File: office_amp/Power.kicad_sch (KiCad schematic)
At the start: 27 parts, among them J1 Jack-DC, Q1 DMT6012LSS, U1 LM74700, U2 TBA_2-2421, U4 TBA_2-2421

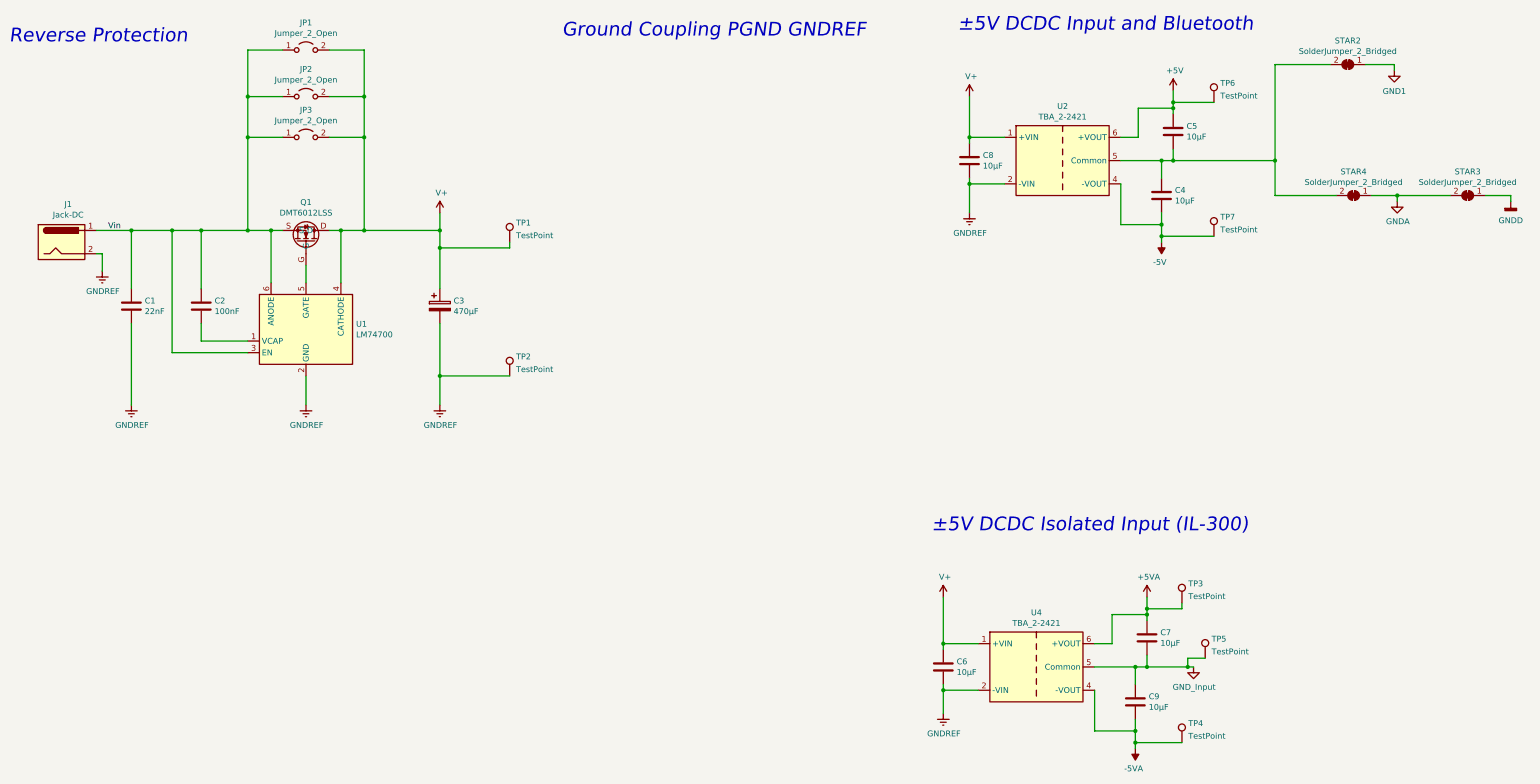
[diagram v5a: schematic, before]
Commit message: Added CHanges from Testing, first layout V1.5
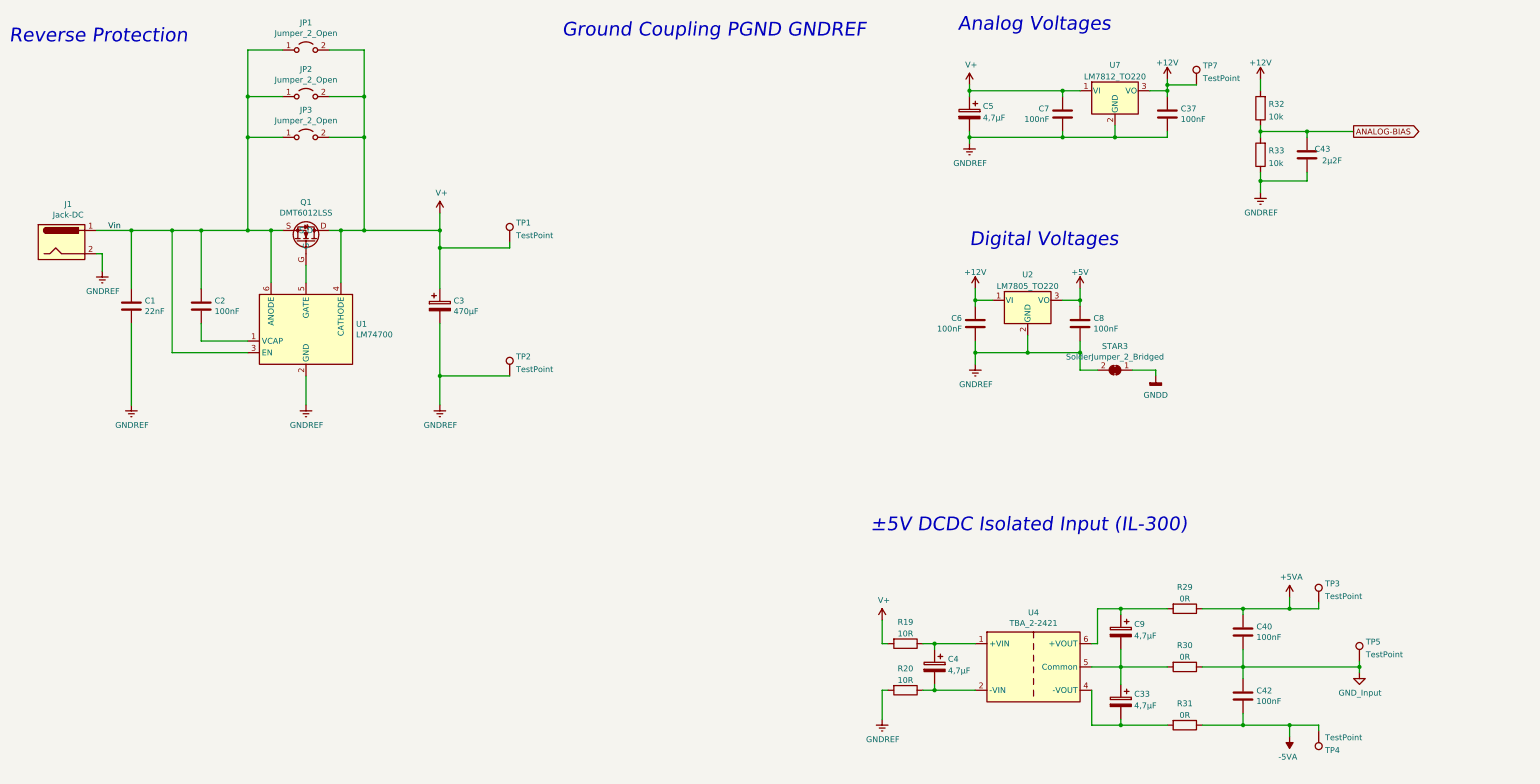
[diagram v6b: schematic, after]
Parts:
- removed C4, C5, C9: 10µF, Capacitor_SMD:C_0805_2012Metric_Pad1.18x1.45mm_HandSolder, symbol Device:C
- removed STAR2, STAR4: SolderJumper_2_Bridged, Jumper:SolderJumper-2_P1.3mm_Bridged_RoundedPad1.0x1.5mm, symbol Jumper:SolderJumper_2_Bridged
- removed TP6: TestPoint, TestPoint:TestPoint_Pad_D1.0mm, symbol Connector:TestPoint
- removed U2: TBA_2-2421, office_amp:SIP-7, symbol MyLib:TBA_2-XXXX
- added C33, C4, C5, C9: 4,7µF, Capacitor_THT:CP_Radial_D5.0mm_P2.00mm, symbol Device:C_Polarized
- added C37, C40, C42: 100nF, Capacitor_SMD:C_0805_2012Metric_Pad1.18x1.45mm_HandSolder, symbol Device:C
- added C43: 2µ2F, Capacitor_SMD:C_0805_2012Metric_Pad1.18x1.45mm_HandSolder, symbol Device:C
- added R19, R20: 10R, Resistor_SMD:R_0805_2012Metric_Pad1.20x1.40mm_HandSolder, symbol Device:R
- added R29, R30, R31: 0R, Resistor_SMD:R_0805_2012Metric_Pad1.20x1.40mm_HandSolder, symbol Device:R
- added R32, R33: 10k, Resistor_SMD:R_0805_2012Metric_Pad1.20x1.40mm_HandSolder, symbol Device:R
- added U2: LM7805_TO220, Package_TO_SOT_THT:TO-220-3_Vertical, symbol Regulator_Linear:LM7805_TO220
- added U7: LM7812_TO220, Package_TO_SOT_THT:TO-220-3_Vertical, symbol Regulator_Linear:LM7812_TO220
- C6, C7, C8: value 10µF -> 100nF
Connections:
- net GNDA is gone; now on net GNDREF: STAR3.2 (B)
- net +5V: now also C8.1, U2.3 (VO)
- net +5VA: now also C40.1, R29.1; no longer C7.1, U4.6 (+VOUT)
- net -5VA: now also C42.2, R31.1; no longer U4.4 (-VOUT)
- net GNDREF: now also C7.2, C37.2, C43.1, C5.2, R20.2, R33.1, U2.2 (GND), U7.2 (GND); no longer U4.2 (-VIN)
- net GND_Input: now also C40.2, C42.1, R30.1; no longer C7.2, U4.5 (Common)
- net V+: now also C7.1, C5.1, R19.2, U7.1 (VI); no longer C6.1, C8.1, U4.1 (+VIN)
- net -5V renamed +12V
- net +12V: now also C6.1, C37.1, R32.2, U2.1 (VI), U7.3 (VO)
- new net: C4.1, R19.1, U4.1 (+VIN)
- new net: C4.2, R20.1, U4.2 (-VIN)
- new net: C33.2, R31.2, U4.4 (-VOUT)
- new net: C33.1, C9.2, R30.2, U4.5 (Common)
- new net: C9.1, R29.2, U4.6 (+VOUT)
- new net ANALOG-BIAS: C43.2, R32.1, R33.2
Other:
- note added: "Analog Voltages"
- note added: "Digital Voltages"
- note removed: "±5V DCDC Input and Bluetooth"
- moved on the sheet: STAR3, TP3, TP4, TP5, TP7, U4

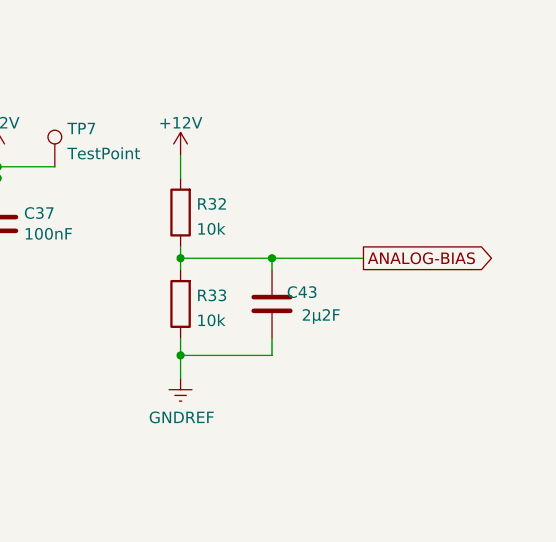
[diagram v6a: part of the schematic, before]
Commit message: Organized Schematic
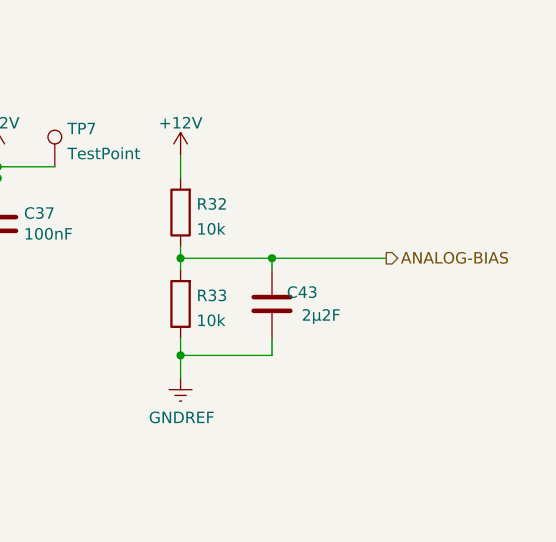
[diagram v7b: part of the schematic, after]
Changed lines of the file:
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@@
   (junction (at 113.03 69.85) (diameter 0) (color 0 0 0 0)
   )
+  (junction (at 302.26 48.26) (diameter 0) (color 0 0 0 0)
+  )
   (junction (at 298.45 177.8) (diameter 0) (color 0 0 0 0)
   )
@@
   (junction (at 260.35 49.53) (diameter 0) (color 0 0 0 0)
   )
-  (junction (at 302.26 48.26) (diameter 0) (color 0 0 0 0)
-  )
   (junction (at 71.12 49.53) (diameter 0) (color 0 0 0 0)
   )
@@
     (stroke (width 0) (type default) (color 0 0 0 0))
   )
-  (wire (pts (xy 302.26 48.26) (xy 312.42 48.26))
-    (stroke (width 0) (type default) (color 0 0 0 0))
-  )
   (wire (pts (xy 292.1 59.055) (xy 292.1 61.595))
     (stroke (width 0) (type default) (color 0 0 0 0))
@@
   )
   (wire (pts (xy 304.8 152.4) (xy 304.8 151.13))
+    (stroke (width 0) (type default) (color 0 0 0 0))
+  )
+  (wire (pts (xy 302.26 48.26) (xy 314.96 48.26))
     (stroke (width 0) (type default) (color 0 0 0 0))
   )
@@
     (effects (font (size 1.27 1.27)) (justify left bottom))
   )
-  (global_label "ANALOG-BIAS" (shape output) (at 312.42 48.26 0) (fields_autoplaced)
+  (hierarchical_label "ANALOG-BIAS" (shape output) (at 314.96 48.26 0)
     (effects (font (size 1.27 1.27)) (justify left))
-    (property "Intersheet References" "${INTERSHEET_REFS}" (id 0) (at 327.6256 48.1806 0)
-      (effects (font (size 1.27 1.27)) (justify left) hide)
-    )
   )
   (symbol (lib_id "Power_Management:LM74700") (at 83.82 91.44 0) (unit 1)

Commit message: new test software
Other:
- moved on the sheet: C43, R32, R33
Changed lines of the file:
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@@
   (junction (at 288.29 152.4) (diameter 0) (color 0 0 0 0)
   )
-  (junction (at 292.1 59.055) (diameter 0) (color 0 0 0 0)
+  (junction (at 299.72 59.055) (diameter 0) (color 0 0 0 0)
   )
   (junction (at 113.03 73.66) (diameter 0) (color 0 0 0 0)
@@
   (junction (at 113.03 69.85) (diameter 0) (color 0 0 0 0)
   )
-  (junction (at 302.26 48.26) (diameter 0) (color 0 0 0 0)
+  (junction (at 309.88 48.26) (diameter 0) (color 0 0 0 0)
   )
   (junction (at 298.45 177.8) (diameter 0) (color 0 0 0 0)
@@
   (junction (at 76.2 69.85) (diameter 0) (color 0 0 0 0)
   )
-  (junction (at 292.1 48.26) (diameter 0) (color 0 0 0 0)
+  (junction (at 299.72 48.26) (diameter 0) (color 0 0 0 0)
   )
   (junction (at 113.03 101.6) (diameter 0) (color 0 0 0 0)
@@
     (stroke (width 0) (type default) (color 0 0 0 0))
   )
-  (wire (pts (xy 292.1 36.83) (xy 292.1 39.37))
+  (wire (pts (xy 299.72 36.83) (xy 299.72 39.37))
     (stroke (width 0) (type default) (color 0 0 0 0))
   )
@@
     (stroke (width 0) (type default) (color 0 0 0 0))
   )
-  (wire (pts (xy 292.1 59.055) (xy 292.1 61.595))
+  (wire (pts (xy 299.72 59.055) (xy 299.72 61.595))
     (stroke (width 0) (type default) (color 0 0 0 0))
   )
@@
     (stroke (width 0) (type default) (color 0 0 0 0))
   )
-  (wire (pts (xy 292.1 46.99) (xy 292.1 48.26))
+  (wire (pts (xy 299.72 46.99) (xy 299.72 48.26))
     (stroke (width 0) (type default) (color 0 0 0 0))
   )
@@
     (stroke (width 0) (type default) (color 0 0 0 0))
   )
-  (wire (pts (xy 302.26 48.26) (xy 302.26 49.53))
-    (stroke (width 0) (type default) (color 0 0 0 0))
-  )
-  (wire (pts (xy 302.26 59.055) (xy 302.26 57.15))
+  (wire (pts (xy 309.88 48.26) (xy 309.88 49.53))
+    (stroke (width 0) (type default) (color 0 0 0 0))
+  )
+  (wire (pts (xy 309.88 59.055) (xy 309.88 57.15))
     (stroke (width 0) (type default) (color 0 0 0 0))
   )
@@
     (stroke (width 0) (type default) (color 0 0 0 0))
   )
-  (wire (pts (xy 302.26 48.26) (xy 314.96 48.26))
+  (wire (pts (xy 309.88 48.26) (xy 322.58 48.26))
     (stroke (width 0) (type default) (color 0 0 0 0))
   )
@@
     (stroke (width 0) (type default) (color 0 0 0 0))
   )
-  (wire (pts (xy 292.1 57.15) (xy 292.1 59.055))
+  (wire (pts (xy 299.72 57.15) (xy 299.72 59.055))
     (stroke (width 0) (type default) (color 0 0 0 0))
   )
@@
     (stroke (width 0) (type default) (color 0 0 0 0))
   )
-  (wire (pts (xy 292.1 59.055) (xy 302.26 59.055))
+  (wire (pts (xy 299.72 59.055) (xy 309.88 59.055))
     (stroke (width 0) (type default) (color 0 0 0 0))
   )
@@
     (stroke (width 0) (type default) (color 0 0 0 0))
   )
-  (wire (pts (xy 292.1 48.26) (xy 292.1 49.53))
-    (stroke (width 0) (type default) (color 0 0 0 0))
-  )
-  (wire (pts (xy 292.1 48.26) (xy 302.26 48.26))
+  (wire (pts (xy 299.72 48.26) (xy 299.72 49.53))
+    (stroke (width 0) (type default) (color 0 0 0 0))
+  )
+  (wire (pts (xy 299.72 48.26) (xy 309.88 48.26))
     (stroke (width 0) (type default) (color 0 0 0 0))
   )
@@
     (effects (font (size 1.27 1.27)) (justify left bottom))
   )
-  (hierarchical_label "ANALOG-BIAS" (shape output) (at 314.96 48.26 0)
+  (hierarchical_label "ANALOG-BIAS" (shape output) (at 322.58 48.26 0)
     (effects (font (size 1.27 1.27)) (justify left))
   )
@@
     (pin "2")
   )
-  (symbol (lib_id "power:GNDREF") (at 292.1 61.595 0) (unit 1)
-    (in_bom yes) (on_board yes)
-    (property "Reference" "#PWR020" (id 0) (at 292.1 67.945 0)
-      (effects (font (size 1.27 1.27)) hide)
-    )
-    (property "Value" "GNDREF" (id 1) (at 292.227 65.9892 0))
-    (property "Footprint" "" (id 2) (at 292.1 61.595 0)
-      (effects (font (size 1.27 1.27)) hide)
-    )
-    (property "Datasheet" "" (id 3) (at 292.1 61.595 0)
+  (symbol (lib_id "power:GNDREF") (at 299.72 61.595 0) (unit 1)
+    (in_bom yes) (on_board yes)
+    (property "Reference" "#PWR020" (id 0) (at 299.72 67.945 0)
+      (effects (font (size 1.27 1.27)) hide)
+    )
+    (property "Value" "GNDREF" (id 1) (at 299.847 65.9892 0))
+    (property "Footprint" "" (id 2) (at 299.72 61.595 0)
+      (effects (font (size 1.27 1.27)) hide)
+    )
+    (property "Datasheet" "" (id 3) (at 299.72 61.595 0)
       (effects (font (size 1.27 1.27)) hide)
     )
@@
     (pin "1")
   )
-  (symbol (lib_id "Device:R") (at 292.1 43.18 180) (unit 1)
-    (in_bom yes) (on_board yes) (fields_autoplaced)
-    (property "Reference" "R32" (id 0) (at 293.878 42.2715 0)
+  (symbol (lib_id "Device:R") (at 299.72 43.18 180) (unit 1)
+    (in_bom yes) (on_board yes) (fields_autoplaced)
+    (property "Reference" "R32" (id 0) (at 301.498 42.2715 0)
       (effects (font (size 1.27 1.27)) (justify right))
     )
-    (property "Value" "10k" (id 1) (at 293.878 45.0466 0)
+    (property "Value" "10k" (id 1) (at 301.498 45.0466 0)
       (effects (font (size 1.27 1.27)) (justify right))
     )
-    (property "Footprint" "Resistor_SMD:R_0805_2012Metric_Pad1.20x1.40mm_HandSolder" (id 2) (at 293.878 43.18 90)
-      (effects (font (size 1.27 1.27)) hide)
-    )
-    (property "Datasheet" "~" (id 3) (at 292.1 43.18 0)
-      (effects (font (size 1.27 1.27)) hide)
-    )
-    (pin "1")
-    (pin "2")
-  )
-  (symbol (lib_id "Device:R") (at 292.1 53.34 180) (unit 1)
-    (in_bom yes) (on_board yes) (fields_autoplaced)
-    (property "Reference" "R33" (id 0) (at 293.878 52.4315 0)
+    (property "Footprint" "Resistor_SMD:R_0805_2012Metric_Pad1.20x1.40mm_HandSolder" (id 2) (at 301.498 43.18 90)
+      (effects (font (size 1.27 1.27)) hide)
+    )
+    (property "Datasheet" "~" (id 3) (at 299.72 43.18 0)
+      (effects (font (size 1.27 1.27)) hide)
+    )
+    (pin "1")
+    (pin "2")
+  )
+  (symbol (lib_id "Device:R") (at 299.72 53.34 180) (unit 1)
+    (in_bom yes) (on_board yes) (fields_autoplaced)
+    (property "Reference" "R33" (id 0) (at 301.498 52.4315 0)
       (effects (font (size 1.27 1.27)) (justify right))
     )
-    (property "Value" "10k" (id 1) (at 293.878 55.2066 0)
+    (property "Value" "10k" (id 1) (at 301.498 55.2066 0)
       (effects (font (size 1.27 1.27)) (justify right))
     )
-    (property "Footprint" "Resistor_SMD:R_0805_2012Metric_Pad1.20x1.40mm_HandSolder" (id 2) (at 293.878 53.34 90)
-      (effects (font (size 1.27 1.27)) hide)
-    )
-    (property "Datasheet" "~" (id 3) (at 292.1 53.34 0)
+    (property "Footprint" "Resistor_SMD:R_0805_2012Metric_Pad1.20x1.40mm_HandSolder" (id 2) (at 301.498 53.34 90)
+      (effects (font (size 1.27 1.27)) hide)
+    )
+    (property "Datasheet" "~" (id 3) (at 299.72 53.34 0)
       (effects (font (size 1.27 1.27)) hide)
     )
@@
     (pin "2")
   )
-  (symbol (lib_id "power:+12V") (at 292.1 36.83 0) (unit 1)
-    (in_bom yes) (on_board yes) (fields_autoplaced)
-    (property "Reference" "#PWR015" (id 0) (at 292.1 40.64 0)
-      (effects (font (size 1.27 1.27)) hide)
-    )
-    (property "Value" "+12V" (id 1) (at 292.1 33.2542 0))
-    (property "Footprint" "" (id 2) (at 292.1 36.83 0)
-      (effects (font (size 1.27 1.27)) hide)
-    )
-    (property "Datasheet" "" (id 3) (at 292.1 36.83 0)
-      (effects (font (size 1.27 1.27)) hide)
-    )
-    (pin "1")
-  )
-  (symbol (lib_id "Device:C") (at 302.26 53.34 180) (unit 1)
-    (in_bom yes) (on_board yes)
-    (property "Reference" "C43" (id 0) (at 307.34 52.07 0)
-      (effects (font (size 1.27 1.27)) (justify left))
-    )
-    (property "Value" "2µ2F" (id 1) (at 309.88 54.61 0)
-      (effects (font (size 1.27 1.27)) (justify left))
-    )
-    (property "Footprint" "Capacitor_SMD:C_0805_2012Metric_Pad1.18x1.45mm_HandSolder" (id 2) (at 301.2948 49.53 0)
-      (effects (font (size 1.27 1.27)) hide)
-    )
-    (property "Datasheet" "~" (id 3) (at 302.26 53.34 0)
-      (effects (font (size 1.27 1.27)) hide)
-    )
+  (symbol (lib_id "power:+12V") (at 299.72 36.83 0) (unit 1)
+    (in_bom yes) (on_board yes) (fields_autoplaced)
+    (property "Reference" "#PWR015" (id 0) (at 299.72 40.64 0)
+      (effects (font (size 1.27 1.27)) hide)
+    )
+    (property "Value" "+12V" (id 1) (at 299.72 33.2542 0))
+    (property "Footprint" "" (id 2) (at 299.72 36.83 0)
+      (effects (font (size 1.27 1.27)) hide)
+    )
+    (property "Datasheet" "" (id 3) (at 299.72 36.83 0)
+      (effects (font (size 1.27 1.27)) hide)
+    )
+    (pin "1")
+  )
+  (symbol (lib_id "Device:C") (at 309.88 53.34 180) (unit 1)
+    (in_bom yes) (on_board yes)
+    (property "Reference" "C43" (id 0) (at 314.96 52.07 0)
+      (effects (font (size 1.27 1.27)) (justify left))
+    )
+    (property "Value" "2µ2F" (id 1) (at 317.5 54.61 0)
+      (effects (font (size 1.27 1.27)) (justify left))
+    )
+    (property "Footprint" "Capacitor_SMD:C_0805_2012Metric_Pad1.18x1.45mm_HandSolder" (id 2) (at 308.9148 49.53 0)
+      (effects (font (size 1.27 1.27)) hide)
+    )
+    (property "Datasheet" "~" (id 3) (at 309.88 53.34 0)
+      (effects (font (size 1.27 1.27)) hide)
+    )
